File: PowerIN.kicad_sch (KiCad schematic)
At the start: 23 parts, among them J4 Vin, Q1 CSD19531Q5A, Q2 CSD19531Q5A, U12 INA238, U3 TPS26631PWP

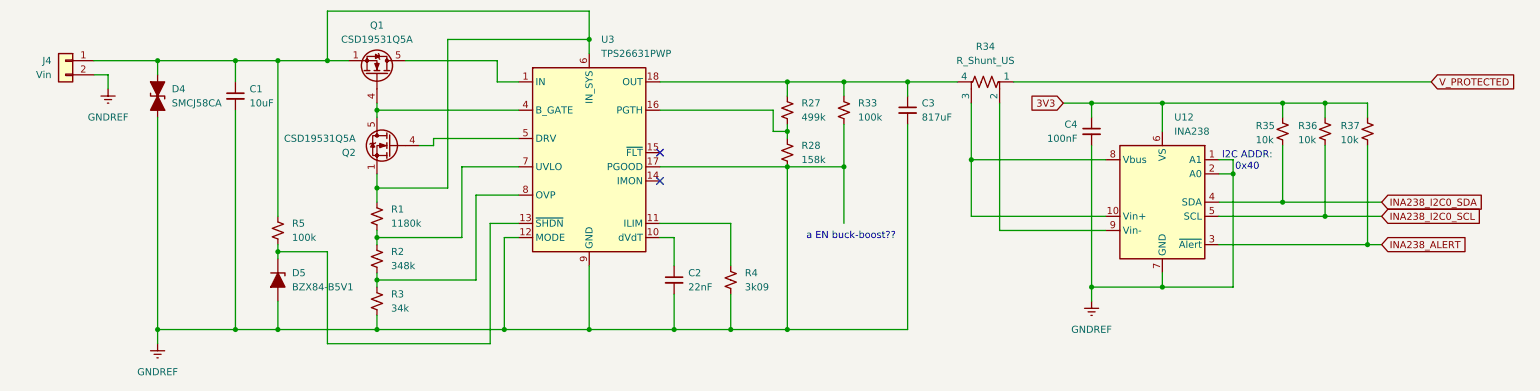
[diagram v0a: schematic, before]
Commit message: updated components and nets
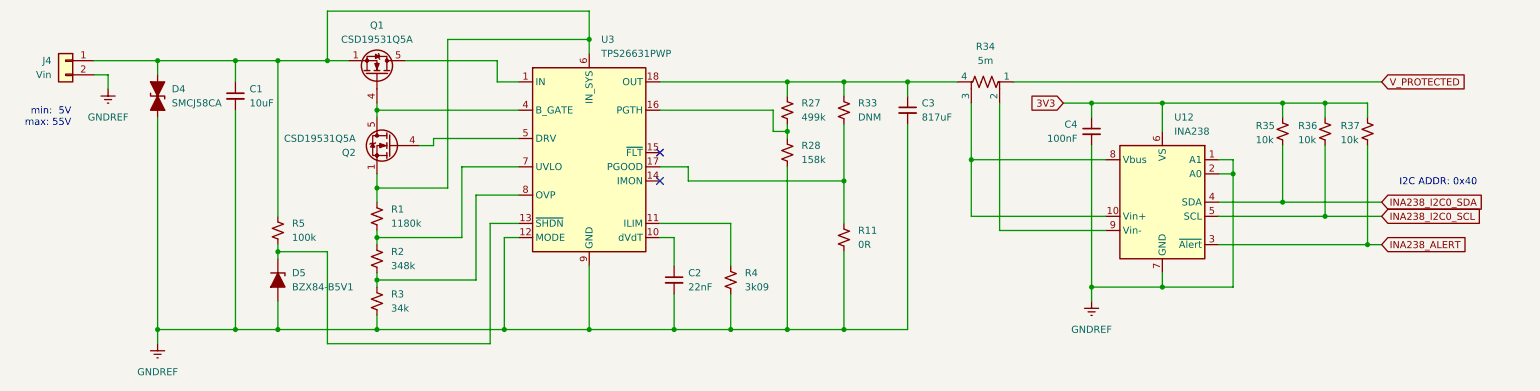
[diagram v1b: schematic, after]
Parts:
- added R11: 0R, symbol Device:R_Small_US
- R33: value 100k -> DNM
- R34: value R_Shunt_US -> 5m
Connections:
- net GNDREF: now also R11.2; no longer R33.2, U3.17 (PGOOD)
- new net: R11.1, R33.2, U3.17 (PGOOD)
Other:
- note added: "min: 5V max: 55V"
- note removed: "a EN buck-boost??"
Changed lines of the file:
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@@
 	(generator_version "9.0")
 	(paper "A4")
-	(text "a EN buck-boost??"
+	(text "min:  5V\nmax: 55V"
 		(exclude_from_sim no)
-		(at 165.1 107.696 0)
+		(at 25.146 86.36 0)
 		(effects
 			(font
 				(size 1.27 1.27)
 			)
+			(justify right)
 		)
 	)
-	(text "I2C ADDR:\n0x40"
+	(text "I2C ADDR: 0x40"
 		(exclude_from_sim no)
-		(at 236.22 94.234 0)
+		(at 270.51 98.044 0)
 		(effects
 			(font
@@
 	)
 	(junction
+		(at 163.83 124.46)
+		(diameter 0)
+		(color 0 0 0 0)
+	)
+	(junction
+		(at 163.83 97.79)
+		(diameter 0)
+		(color 0 0 0 0)
+	)
+	(junction
 		(at 40.64 124.46)
 		(diameter 0)
@@
 	)
 	(junction
-		(at 163.83 95.25)
-		(diameter 0)
-		(color 0 0 0 0)
-	)
-	(junction
 		(at 220.98 83.82)
 		(diameter 0)
@@
 	)
 	(junction
-		(at 153.67 95.25)
-		(diameter 0)
-		(color 0 0 0 0)
-	)
-	(junction
 		(at 186.69 93.98)
 		(diameter 0)
@@
 	(wire
 		(pts
-			(xy 175.26 124.46) (xy 153.67 124.46)
+			(xy 175.26 124.46) (xy 163.83 124.46)
 		)
 		(stroke
@@
 	(wire
 		(pts
+			(xy 135.89 95.25) (xy 130.81 95.25)
+		)
+		(stroke
+			(width 0)
+			(type default)
+		)
+	)
+	(wire
+		(pts
 			(xy 175.26 80.01) (xy 184.15 80.01)
 		)
@@
 	(wire
 		(pts
-			(xy 163.83 95.25) (xy 163.83 87.63)
+			(xy 163.83 87.63) (xy 163.83 97.79)
 		)
 		(stroke
@@
 	(wire
 		(pts
-			(xy 102.87 124.46) (xy 118.11 124.46)
+			(xy 163.83 97.79) (xy 163.83 105.41)
 		)
 		(stroke
@@
 	(wire
 		(pts
-			(xy 130.81 80.01) (xy 153.67 80.01)
+			(xy 102.87 124.46) (xy 118.11 124.46)
 		)
 		(stroke
@@
 	(wire
 		(pts
-			(xy 186.69 83.82) (xy 186.69 93.98)
+			(xy 130.81 80.01) (xy 153.67 80.01)
 		)
 		(stroke
@@
 	(wire
 		(pts
-			(xy 153.67 95.25) (xy 163.83 95.25)
+			(xy 186.69 83.82) (xy 186.69 93.98)
 		)
 		(stroke
@@
 	(wire
 		(pts
+			(xy 135.89 97.79) (xy 163.83 97.79)
+		)
+		(stroke
+			(width 0)
+			(type default)
+		)
+	)
+	(wire
+		(pts
 			(xy 71.12 67.31) (xy 118.11 67.31)
 		)
@@
 	(wire
 		(pts
-			(xy 194.31 80.01) (xy 269.24 80.01)
+			(xy 194.31 80.01) (xy 260.35 80.01)
 		)
 		(stroke
@@
 	(wire
 		(pts
-			(xy 242.57 83.82) (xy 242.57 86.36)
+			(xy 163.83 124.46) (xy 153.67 124.46)
 		)
 		(stroke
@@
 	(wire
 		(pts
-			(xy 80.01 85.09) (xy 80.01 86.36)
+			(xy 242.57 83.82) (xy 242.57 86.36)
 		)
 		(stroke
@@
 	(wire
 		(pts
-			(xy 80.01 96.52) (xy 80.01 99.06)
+			(xy 80.01 85.09) (xy 80.01 86.36)
 		)
 		(stroke
@@
 	(wire
 		(pts
-			(xy 54.61 124.46) (xy 62.23 124.46)
+			(xy 80.01 96.52) (xy 80.01 99.06)
 		)
 		(stroke
@@
 	(wire
 		(pts
-			(xy 31.75 78.74) (xy 29.21 78.74)
+			(xy 54.61 124.46) (xy 62.23 124.46)
 		)
 		(stroke
@@
 	(wire
 		(pts
-			(xy 220.98 83.82) (xy 220.98 88.9)
+			(xy 31.75 78.74) (xy 29.21 78.74)
 		)
 		(stroke
@@
 	(wire
 		(pts
-			(xy 250.19 91.44) (xy 250.19 104.14)
+			(xy 220.98 83.82) (xy 220.98 88.9)
 		)
 		(stroke
@@
 	(wire
 		(pts
-			(xy 62.23 76.2) (xy 71.12 76.2)
+			(xy 250.19 91.44) (xy 250.19 104.14)
 		)
 		(stroke
@@
 	(wire
 		(pts
-			(xy 163.83 95.25) (xy 163.83 105.41)
+			(xy 62.23 76.2) (xy 71.12 76.2)
 		)
 		(stroke
@@
 	(wire
 		(pts
+			(xy 163.83 110.49) (xy 163.83 124.46)
+		)
+		(stroke
+			(width 0)
+			(type default)
+		)
+	)
+	(wire
+		(pts
 			(xy 95.25 107.95) (xy 80.01 107.95)
 		)
@@
 	(wire
 		(pts
-			(xy 130.81 95.25) (xy 153.67 95.25)
+			(xy 135.89 97.79) (xy 135.89 95.25)
 		)
 		(stroke
@@
 	(global_label "V_PROTECTED"
 		(shape input)
-		(at 269.24 80.01 0)
+		(at 260.35 80.01 0)
 		(fields_autoplaced yes)
 		(effects
@@
 		)
 		(property "Intersheetrefs" "${INTERSHEET_REFS}"
-			(at 284.9251 80.01 0)
+			(at 276.0351 80.01 0)
 			(effects
 				(font
@@
 			)
 		)
-		(property "Value" "R_Shunt_US"
+		(property "Value" "5m"
 			(at 189.23 76.2 90)
 			(effects
@@
 			)
 		)
-		(property "Datasheet" "~"
+		(property "Datasheet" "Vishay WSLP2512R0050FEA"
 			(at 189.23 80.01 0)
 			(effects
@@
 	(symbol
 		(lib_id "Device:R_Small_US")
+		(at 163.83 107.95 0)
+		(unit 1)
+		(exclude_from_sim no)
+		(in_bom yes)
+		(on_board yes)
+		(dnp no)
+		(fields_autoplaced yes)
+		(property "Reference" "R11"
+			(at 166.37 106.6799 0)
+			(effects
+				(font
+					(size 1.27 1.27)
+				)
+				(justify left)
+			)
+		)
+		(property "Value" "0R"
+			(at 166.37 109.2199 0)
+			(effects
+				(font
+					(size 1.27 1.27)
+				)
+				(justify left)
+			)
+		)
+		(property "Footprint" ""
+			(at 163.83 107.95 0)
+			(effects
+				(font
+					(size 1.27 1.27)
+				)
+				(hide yes)
+			)
+		)
+		(property "Datasheet" "~"
+			(at 163.83 107.95 0)
+			(effects
+				(font
+					(size 1.27 1.27)
+				)
+				(hide yes)
+			)
+		)
+		(property "Description" "Resistor, small US symbol"
+			(at 163.83 107.95 0)
+			(effects
+				(font
+					(size 1.27 1.27)
+				)
+				(hide yes)
+			)
+		)
+		(pin "1"
+		)
+		(pin "2"
+		)
+		(instances
+			(project "Navigator S1"
+				(path "/c978ef74-ad4b-4bd0-81cb-39647b7420fd/c16e2143-82a2-46cd-8ab3-14f654996ee5"
+					(reference "R11")
+					(unit 1)
+				)
+			)
+		)
+	)
+	(symbol
+		(lib_id "Device:R_Small_US")
 		(at 163.83 85.09 0)
 		(unit 1)
@@
 			)
 		)
-		(property "Value" "100k"
+		(property "Value" "DNM"
 			(at 166.37 86.3599 0)
 			(effects
